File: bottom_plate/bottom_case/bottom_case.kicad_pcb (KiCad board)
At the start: 2 copper layers, 134.2 x 107.2 mm, 0 parts

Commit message: updated
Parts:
- added REF**: MountingHole_2.2mm_M2_DIN965_Pad, MountingHole:MountingHole_2.2mm_M2_DIN965_Pad, F.Cu at (87.7, 10.0)
- added REF**: MountingHole_2.2mm_M2_DIN965_Pad, MountingHole:MountingHole_2.2mm_M2_DIN965_Pad, F.Cu at (87.7, 67.2)
- added REF**: MountingHole_2.2mm_M2_DIN965_Pad, MountingHole:MountingHole_2.2mm_M2_DIN965_Pad, F.Cu at (9.53, 66.7)
- added REF**: MountingHole_2.2mm_M2_DIN965_Pad, MountingHole:MountingHole_2.2mm_M2_DIN965_Pad, F.Cu at (47.6, 41.1)
- added REF**: MountingHole_2.2mm_M2_DIN965_Pad, MountingHole:MountingHole_2.2mm_M2_DIN965_Pad, F.Cu at (9.25, 9.25)
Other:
- outline, holes or cut-outs redrawn

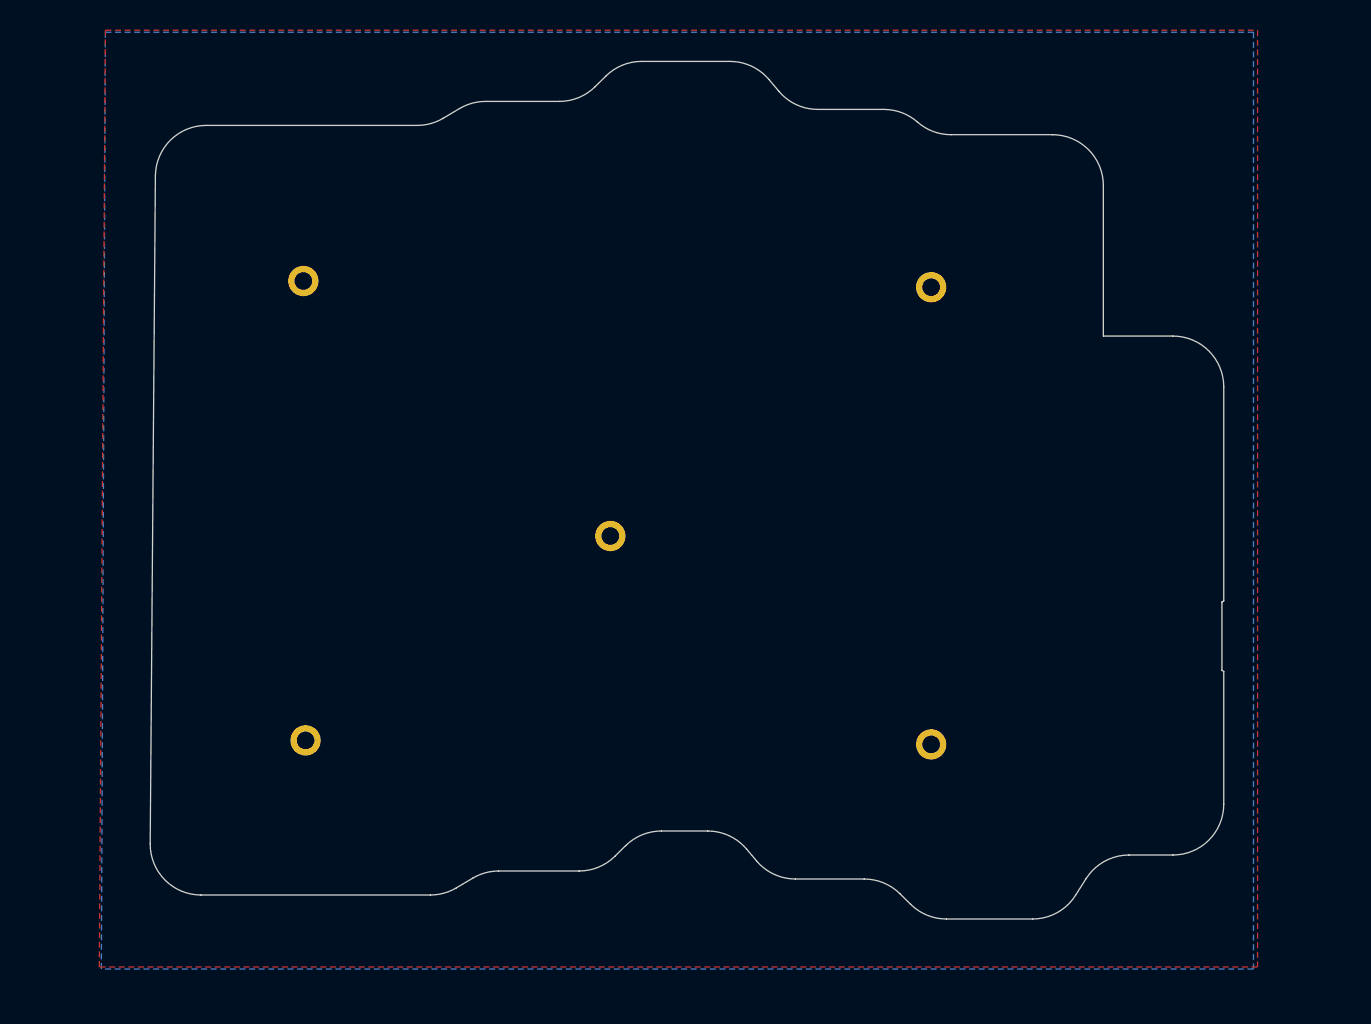
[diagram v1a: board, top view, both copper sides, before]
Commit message: fix bottom case hole alignment
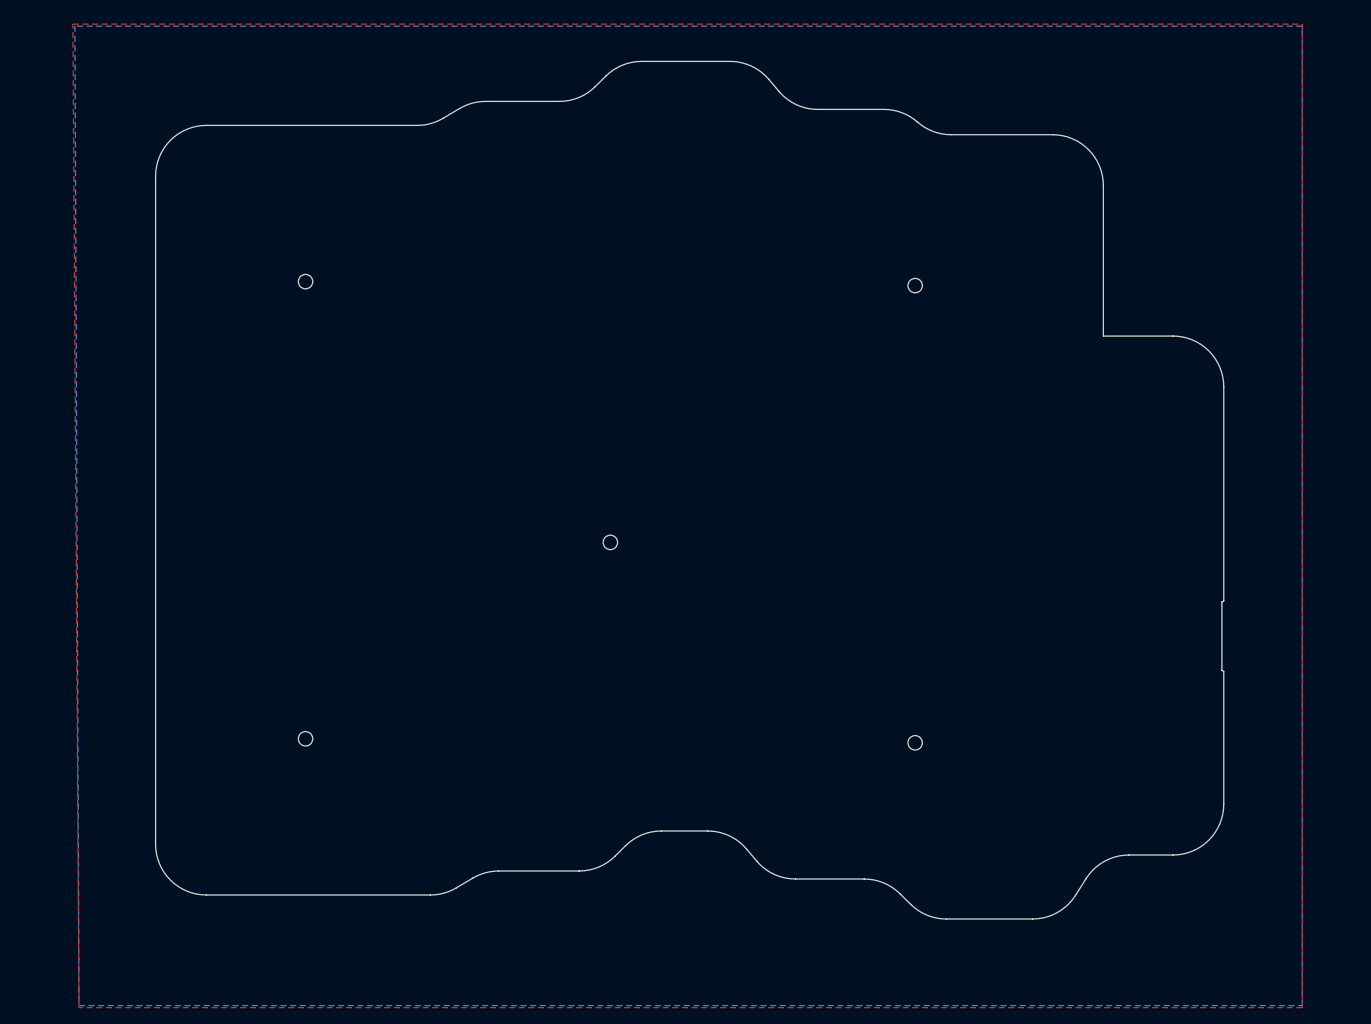
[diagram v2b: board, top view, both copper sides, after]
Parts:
- removed REF** (x5): MountingHole_2.2mm_M2_DIN965_Pad, MountingHole:MountingHole_2.2mm_M2_DIN965_Pad
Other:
- board size 134.2 x 107.2 mm -> 133.5 x 107.2 mm
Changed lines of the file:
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@@
   (general
     (thickness 1.6)
-    (drawings 50)
+    (drawings 55)
     (tracks 0)
     (zones 0)
-    (modules 5)
+    (modules 0)
     (nets 1)
   )
@@
     (uvia_drill 0.1)
   )
-  (module MountingHole:MountingHole_2.2mm_M2_DIN965_Pad (layer F.Cu)
-    (at 87.725 10.025)
-    (descr "Mounting Hole 2.2mm, M2, DIN965")
-    (tags "mounting hole 2.2mm m2 din965")
-    (attr virtual)
-    (fp_text reference REF** (at 0 -2.9) (layer F.SilkS) hide
-      (effects (font (size 1 1) (thickness 0.15)))
-    )
-    (fp_text value MountingHole_2.2mm_M2_DIN965_Pad (at 0 2.9) (layer F.Fab)
-      (effects (font (size 1 1) (thickness 0.15)))
-    )
-    (fp_text user %R (at 0.3 0) (layer F.Fab)
-      (effects (font (size 1 1) (thickness 0.15)))
-    )
-    (fp_circle (center 0 0) (end 1.9 0) (layer Cmts.User) (width 0.15))
-    (fp_circle (center 0 0) (end 2.15 0) (layer F.CrtYd) (width 0.05))
-    (pad 1 thru_hole circle (at 0 0) (size 3.8 3.8) (drill 2.2) (layers *.Cu *.Mask))
-  )
-  (module MountingHole:MountingHole_2.2mm_M2_DIN965_Pad (layer F.Cu)
-    (at 87.725 67.175)
-    (descr "Mounting Hole 2.2mm, M2, DIN965")
-    (tags "mounting hole 2.2mm m2 din965")
-    (attr virtual)
-    (fp_text reference REF** (at 0 -2.9) (layer F.SilkS) hide
-      (effects (font (size 1 1) (thickness 0.15)))
-    )
-    (fp_text value MountingHole_2.2mm_M2_DIN965_Pad (at 0 2.9) (layer F.Fab)
-      (effects (font (size 1 1) (thickness 0.15)))
-    )
-    (fp_text user %R (at 0.3 0) (layer F.Fab)
-      (effects (font (size 1 1) (thickness 0.15)))
-    )
-    (fp_circle (center 0 0) (end 1.9 0) (layer Cmts.User) (width 0.15))
-    (fp_circle (center 0 0) (end 2.15 0) (layer F.CrtYd) (width 0.05))
-    (pad 1 thru_hole circle (at 0 0) (size 3.8 3.8) (drill 2.2) (layers *.Cu *.Mask))
-  )
-  (module MountingHole:MountingHole_2.2mm_M2_DIN965_Pad (layer F.Cu)
-    (at 9.525 66.675)
-    (descr "Mounting Hole 2.2mm, M2, DIN965")
-    (tags "mounting hole 2.2mm m2 din965")
-    (attr virtual)
-    (fp_text reference REF** (at 0 -2.9) (layer F.SilkS) hide
-      (effects (font (size 1 1) (thickness 0.15)))
-    )
-    (fp_text value MountingHole_2.2mm_M2_DIN965_Pad (at 0 2.9) (layer F.Fab)
-      (effects (font (size 1 1) (thickness 0.15)))
-    )
-    (fp_text user %R (at 0.3 0) (layer F.Fab)
-      (effects (font (size 1 1) (thickness 0.15)))
-    )
-    (fp_circle (center 0 0) (end 1.9 0) (layer Cmts.User) (width 0.15))
-    (fp_circle (center 0 0) (end 2.15 0) (layer F.CrtYd) (width 0.05))
-    (pad 1 thru_hole circle (at 0 0) (size 3.8 3.8) (drill 2.2) (layers *.Cu *.Mask))
-  )
-  (module MountingHole:MountingHole_2.2mm_M2_DIN965_Pad (layer F.Cu)
-    (at 47.625 41.125)
-    (descr "Mounting Hole 2.2mm, M2, DIN965")
-    (tags "mounting hole 2.2mm m2 din965")
-    (attr virtual)
-    (fp_text reference REF** (at 0 -2.9) (layer F.SilkS) hide
-      (effects (font (size 1 1) (thickness 0.15)))
-    )
-    (fp_text value MountingHole_2.2mm_M2_DIN965_Pad (at 0 2.9) (layer F.Fab)
-      (effects (font (size 1 1) (thickness 0.15)))
-    )
-    (fp_text user %R (at 0.3 0) (layer F.Fab) hide
-      (effects (font (size 1 1) (thickness 0.15)))
-    )
-    (fp_circle (center 0 0) (end 1.9 0) (layer Cmts.User) (width 0.15))
-    (fp_circle (center 0 0) (end 2.15 0) (layer F.CrtYd) (width 0.05))
-    (pad 1 thru_hole circle (at 0 0) (size 3.8 3.8) (drill 2.2) (layers *.Cu *.Mask))
-  )
-  (module MountingHole:MountingHole_2.2mm_M2_DIN965_Pad (layer F.Cu)
-    (at 9.25 9.25)
-    (descr "Mounting Hole 2.2mm, M2, DIN965")
-    (tags "mounting hole 2.2mm m2 din965")
-    (attr virtual)
-    (fp_text reference REF** (at 0 -2.9) (layer F.SilkS) hide
-      (effects (font (size 1 1) (thickness 0.15)))
-    )
-    (fp_text value MountingHole_2.2mm_M2_DIN965_Pad (at 0 2.9) (layer F.Fab)
-      (effects (font (size 1 1) (thickness 0.15)))
-    )
-    (fp_circle (center 0 0) (end 2.15 0) (layer F.CrtYd) (width 0.05))
-    (fp_circle (center 0 0) (end 1.9 0) (layer Cmts.User) (width 0.15))
-    (fp_text user %R (at 0.3 0) (layer F.Fab)
-      (effects (font (size 1 1) (thickness 0.15)))
-    )
-    (pad 1 thru_hole circle (at 0 0) (size 3.8 3.8) (drill 2.2) (layers *.Cu *.Mask))
-  )
-  (gr_line (start 23.482231 -10.2) (end -2.895436 -10.2) (layer Edge.Cuts) (width 0.05))
+  (gr_circle (center 85.725 9.825) (end 86.625 9.825) (layer Edge.Cuts) (width 0.05))
+  (gr_circle (center 47.625 41.925) (end 48.525 41.925) (layer Edge.Cuts) (width 0.05))
+  (gr_circle (center 9.525 9.324999) (end 10.425 9.324999) (layer Edge.Cuts) (width 0.05))
+  (gr_circle (center 9.525 66.474999) (end 10.425 66.474999) (layer Edge.Cuts) (width 0.05))
+  (gr_circle (center 85.725 66.975) (end 86.625 66.975) (layer Edge.Cuts) (width 0.05))
+  (gr_line (start 23.482231 -10.2) (end -2.871925 -10.2) (layer Edge.Cuts) (width 0.05))
   (gr_arc (start 23.482231 -16.549999) (end 23.482231 -10.2) (angle -30.71282772) (layer Edge.Cuts) (width 0.05))
   (gr_line (start 28.776832 -12.309335) (end 26.725401 -11.090664) (layer Edge.Cuts) (width 0.05))
@@
   (gr_line (start 28.373167 85.109335) (end 30.424598 83.890664) (layer Edge.Cuts) (width 0.05))
   (gr_arc (start 25.129997 79.649999) (end 25.129997 86) (angle -30.71282772) (layer Edge.Cuts) (width 0.05))
-  (gr_line (start -3.545296 86) (end 25.129997 86) (layer Edge.Cuts) (width 0.05))
-  (gr_arc (start -3.545296 79.65) (end -9.895104 79.600581) (angle -90.44590992) (layer Edge.Cuts) (width 0.05))
-  (gr_line (start -9.245244 -3.899418) (end -9.895104 79.600581) (layer Edge.Cuts) (width 0.05))
-  (gr_arc (start -2.895436 -3.85) (end -2.895436 -10.2) (angle -89.55409008) (layer Edge.Cuts) (width 0.05))
+  (gr_line (start -2.871925 86) (end 25.129997 86) (layer Edge.Cuts) (width 0.05))
+  (gr_arc (start -2.871925 79.65) (end -9.221925 79.65) (angle -90) (layer Edge.Cuts) (width 0.05))
+  (gr_line (start -9.221925 -3.85) (end -9.221925 79.65) (layer Edge.Cuts) (width 0.05))
+  (gr_arc (start -2.871925 -3.85) (end -2.871925 -10.2) (angle -90) (layer Edge.Cuts) (width 0.05))
   (zone (net 0) (net_name "") (layer F.Cu) (hatch edge 0.508)
     (connect_pads (clearance 0.508))
@@
     (polygon
       (pts
-        (xy -15.494 -22.098) (xy 128.524 -22.098) (xy 128.524 94.996) (xy -16.256 94.996)
+        (xy -19.558 -22.86) (xy 134.112 -22.86) (xy 134.112 100.076) (xy -18.796 100.076)
       )
     )
@@
     (polygon
       (pts
-        (xy -15.494 -21.844) (xy 128.016 -21.844) (xy 128.016 95.25) (xy -16.002 95.25)
+        (xy -18.796 99.822) (xy 134.112 99.822) (xy 134.112 -22.606) (xy -19.304 -22.606)
       )
     )
